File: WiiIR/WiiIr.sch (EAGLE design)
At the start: 18 parts

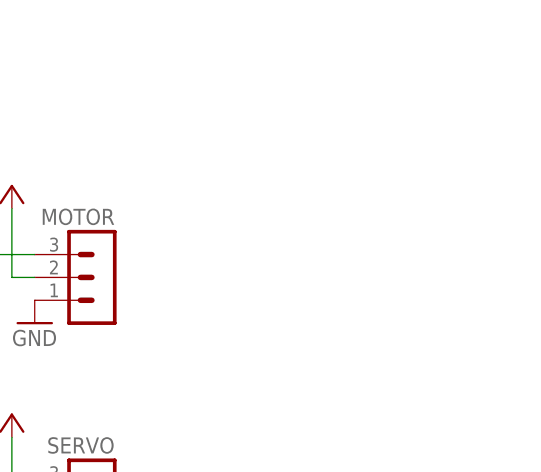
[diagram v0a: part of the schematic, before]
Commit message: XMC Shield servo caps
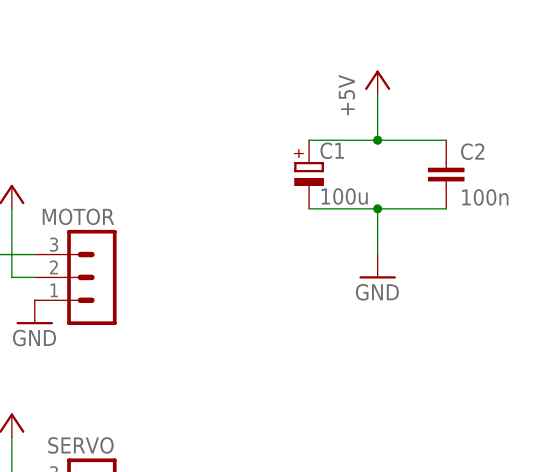
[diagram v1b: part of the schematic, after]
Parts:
- added C1: 100u, resistor:CPOL-EUE2.5-7
- added C2: 100n, resistor:C-EU050-024X044
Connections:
- net +5V: now also C1.+, C2.1
- net GND: now also C1.-, C2.2
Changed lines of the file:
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@@
 <part name="DBG8" library="led" deviceset="LED" device="SQR2X5"/>
 <part name="GND11" library="supply1" deviceset="GND" device=""/>
+<part name="P+5" library="supply1" deviceset="+5V" device=""/>
+<part name="GND6" library="supply1" deviceset="GND" device=""/>
+<part name="C1" library="resistor" deviceset="CPOL-EU" device="E2.5-7" value="100u"/>
+<part name="C2" library="resistor" deviceset="C-EU" device="050-024X044" value="100n"/>
 </parts>
 <sheets>
@@
 <instance part="DBG8" gate="G$1" x="157.48" y="40.64"/>
 <instance part="GND11" gate="1" x="129.54" y="10.16"/>
+<instance part="P+5" gate="1" x="236.22" y="165.1"/>
+<instance part="GND6" gate="1" x="236.22" y="142.24"/>
+<instance part="C1" gate="G$1" x="228.6" y="154.94"/>
+<instance part="C2" gate="G$1" x="243.84" y="154.94"/>
 </instances>
 <busses>
@@
 <wire x1="137.16" y1="149.86" x2="144.78" y2="149.86" width="0.1524" layer="91"/>
 <wire x1="144.78" y1="149.86" x2="144.78" y2="157.48" width="0.1524" layer="91"/>
+</segment>
+<segment>
+<pinref part="C1" gate="G$1" pin="+"/>
+<pinref part="P+5" gate="1" pin="+5V"/>
+<wire x1="228.6" y1="157.48" x2="236.22" y2="157.48" width="0.1524" layer="91"/>
+<wire x1="236.22" y1="157.48" x2="236.22" y2="162.56" width="0.1524" layer="91"/>
+<pinref part="C2" gate="G$1" pin="1"/>
+<wire x1="243.84" y1="157.48" x2="236.22" y2="157.48" width="0.1524" layer="91"/>
+<junction x="236.22" y="157.48"/>
 </segment>
 </net>
@@
 <pinref part="GND11" gate="1" pin="GND"/>
 </segment>
+<segment>
+<pinref part="GND6" gate="1" pin="GND"/>
+<pinref part="C1" gate="G$1" pin="-"/>
+<wire x1="236.22" y1="144.78" x2="236.22" y2="149.86" width="0.1524" layer="91"/>
+<wire x1="236.22" y1="149.86" x2="228.6" y2="149.86" width="0.1524" layer="91"/>
+<pinref part="C2" gate="G$1" pin="2"/>
+<wire x1="243.84" y1="149.86" x2="236.22" y2="149.86" width="0.1524" layer="91"/>
+<junction x="236.22" y="149.86"/>
+</segment>
 </net>

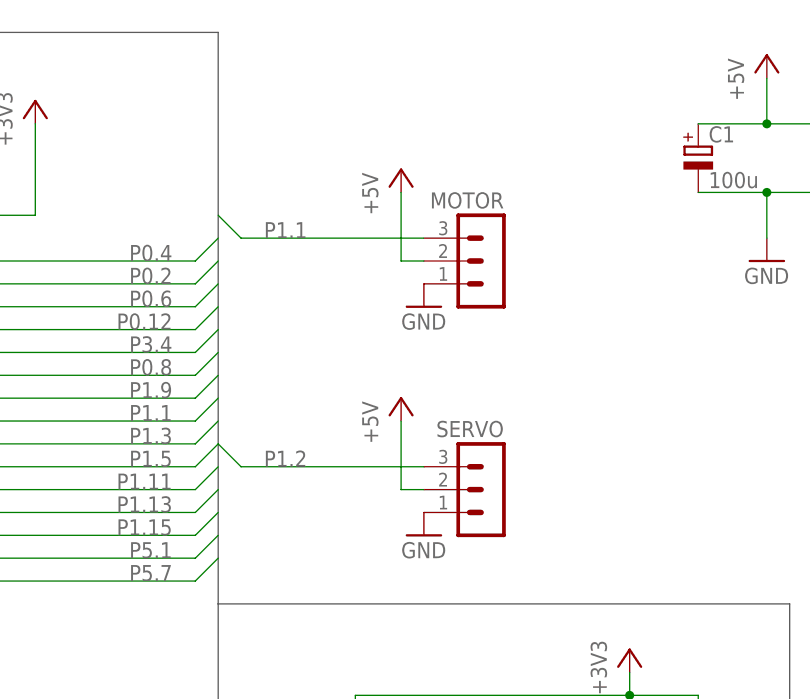
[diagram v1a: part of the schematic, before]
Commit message: Bent pin headers for servo
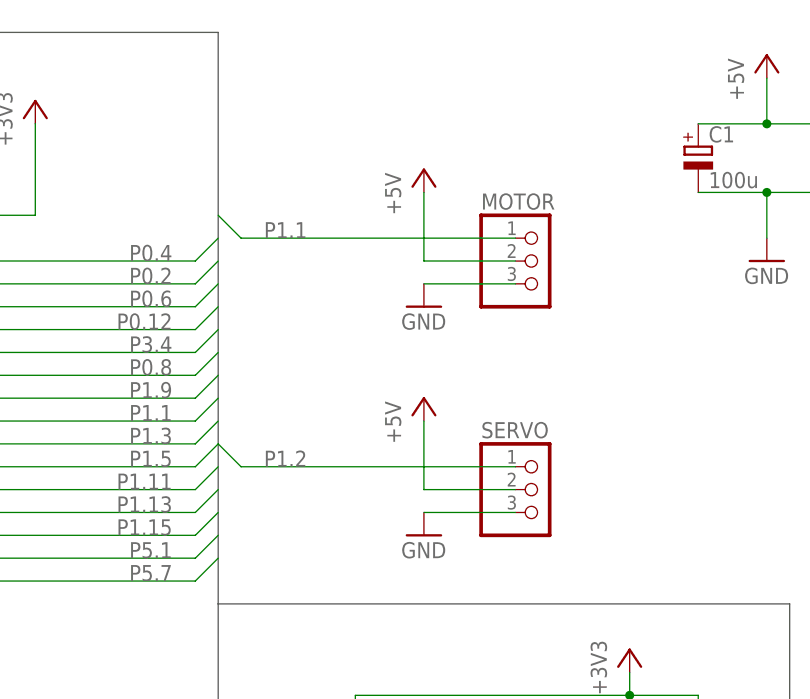
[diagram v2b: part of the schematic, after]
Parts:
- MOTOR, SERVO: device con-lstb:MA03-1 -> pinhead:PINHD-1X3/90
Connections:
- net GND: now also MOTOR.3, SERVO.3; no longer MOTOR.1, SERVO.1
- net P1.1: now also MOTOR.1; no longer MOTOR.3
- net P1.2: now also SERVO.1; no longer SERVO.3
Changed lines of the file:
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@@
 <grid distance="0.1" unitdist="inch" unit="inch" style="lines" multiple="1" display="no" altdistance="0.01" altunitdist="inch" altunit="inch"/>
 <layers>
-<layer number="1" name="Top" color="4" fill="1" visible="no" active="no"/>
-<layer number="16" name="Bottom" color="1" fill="1" visible="no" active="no"/>
-<layer number="17" name="Pads" color="2" fill="1" visible="no" active="no"/>
-<layer number="18" name="Vias" color="2" fill="1" visible="no" active="no"/>
-<layer number="19" name="Unrouted" color="6" fill="1" visible="no" active="no"/>
-<layer number="20" name="Dimension" color="15" fill="1" visible="no" active="no"/>
-<layer number="21" name="tPlace" color="7" fill="1" visible="no" active="no"/>
-<layer number="22" name="bPlace" color="7" fill="1" visible="no" active="no"/>
-<layer number="23" name="tOrigins" color="15" fill="1" visible="no" active="no"/>
-<layer number="24" name="bOrigins" color="15" fill="1" visible="no" active="no"/>
-<layer number="25" name="tNames" color="7" fill="1" visible="no" active="no"/>
-<layer number="26" name="bNames" color="7" fill="1" visible="no" active="no"/>
-<layer number="27" name="tValues" color="7" fill="1" visible="no" active="no"/>
-<layer number="28" name="bValues" color="7" fill="1" visible="no" active="no"/>
+<layer number="1" name="Top" color="4" fill="1" visible="yes" active="no"/>
+<layer number="16" name="Bottom" color="1" fill="1" visible="yes" active="no"/>
+<layer number="17" name="Pads" color="2" fill="1" visible="yes" active="no"/>
+<layer number="18" name="Vias" color="2" fill="1" visible="yes" active="no"/>
+<layer number="19" name="Unrouted" color="6" fill="1" visible="yes" active="no"/>
+<layer number="20" name="Dimension" color="15" fill="1" visible="yes" active="no"/>
+<layer number="21" name="tPlace" color="7" fill="1" visible="yes" active="no"/>
+<layer number="22" name="bPlace" color="7" fill="1" visible="yes" active="no"/>
+<layer number="23" name="tOrigins" color="15" fill="1" visible="yes" active="no"/>
+<layer number="24" name="bOrigins" color="15" fill="1" visible="yes" active="no"/>
+<layer number="25" name="tNames" color="7" fill="1" visible="yes" active="no"/>
+<layer number="26" name="bNames" color="7" fill="1" visible="yes" active="no"/>
+<layer number="27" name="tValues" color="7" fill="1" visible="yes" active="no"/>
+<layer number="28" name="bValues" color="7" fill="1" visible="yes" active="no"/>
 <layer number="29" name="tStop" color="7" fill="3" visible="no" active="no"/>
 <layer number="30" name="bStop" color="7" fill="6" visible="no" active="no"/>
@@
 <layer number="35" name="tGlue" color="7" fill="4" visible="no" active="no"/>
 <layer number="36" name="bGlue" color="7" fill="5" visible="no" active="no"/>
-<layer number="37" name="tTest" color="7" fill="1" visible="no" active="no"/>
-<layer number="38" name="bTest" color="7" fill="1" visible="no" active="no"/>
+<layer number="37" name="tTest" color="7" fill="1" visible="yes" active="no"/>
+<layer number="38" name="bTest" color="7" fill="1" visible="yes" active="no"/>
 <layer number="39" name="tKeepout" color="4" fill="11" visible="no" active="no"/>
 <layer number="40" name="bKeepout" color="1" fill="11" visible="no" active="no"/>
@@
 <layer number="44" name="Drills" color="7" fill="1" visible="no" active="no"/>
 <layer number="45" name="Holes" color="7" fill="1" visible="no" active="no"/>
-<layer number="46" name="Milling" color="3" fill="1" visible="no" active="no"/>
-<layer number="47" name="Measures" color="7" fill="1" visible="no" active="no"/>
-<layer number="48" name="Document" color="7" fill="1" visible="no" active="no"/>
-<layer number="49" name="Reference" color="7" fill="1" visible="no" active="no"/>
-<layer number="51" name="tDocu" color="7" fill="1" visible="no" active="no"/>
-<layer number="52" name="bDocu" color="7" fill="1" visible="no" active="no"/>
+<layer number="46" name="Milling" color="3" fill="1" visible="yes" active="no"/>
+<layer number="47" name="Measures" color="7" fill="1" visible="yes" active="no"/>
+<layer number="48" name="Document" color="7" fill="1" visible="yes" active="no"/>
+<layer number="49" name="Reference" color="7" fill="1" visible="yes" active="no"/>
+<layer number="51" name="tDocu" color="7" fill="1" visible="yes" active="no"/>
+<layer number="52" name="bDocu" color="7" fill="1" visible="yes" active="no"/>
 <layer number="91" name="Nets" color="2" fill="1" visible="yes" active="yes"/>
 <layer number="92" name="Busses" color="1" fill="1" visible="yes" active="yes"/>
@@
 <part name="P+4" library="supply1" deviceset="+5V" device=""/>
 <part name="IR_CAM" library="con-harting-ml" deviceset="ML10" device=""/>
-<part name="MOTOR" library="con-lstb" deviceset="MA03-1" device=""/>
 <part name="FRAME1" library="frames" deviceset="A4L-LOC" device=""/>
 <part name="GND7" library="supply1" deviceset="GND" device=""/>
 <part name="P+9" library="supply1" deviceset="+5V" device=""/>
-<part name="SERVO" library="con-lstb" deviceset="MA03-1" device=""/>
 <part name="GND10" library="supply1" deviceset="GND" device=""/>
 <part name="P+11" library="supply1" deviceset="+5V" device=""/>
@@
 <part name="C1" library="resistor" deviceset="CPOL-EU" device="E2.5-7" value="100u"/>
 <part name="C2" library="resistor" deviceset="C-EU" device="050-024X044" value="100n"/>
+<part name="MOTOR" library="pinhead" deviceset="PINHD-1X3" device="/90"/>
+<part name="SERVO" library="pinhead" deviceset="PINHD-1X3" device="/90"/>
 </parts>
 <sheets>
@@
 <instance part="P+4" gate="1" x="144.78" y="160.02"/>
 <instance part="IR_CAM" gate="G$1" x="205.74" y="78.74"/>
-<instance part="MOTOR" gate="G$1" x="205.74" y="142.24" rot="MR0"/>
 <instance part="FRAME1" gate="G$1" x="0" y="0"/>
 <instance part="GND7" gate="1" x="198.12" y="137.16"/>
-<instance part="P+9" gate="1" x="195.58" y="152.4"/>
-<instance part="SERVO" gate="G$1" x="205.74" y="116.84" rot="MR0"/>
+<instance part="P+9" gate="1" x="198.12" y="152.4"/>
 <instance part="GND10" gate="1" x="198.12" y="111.76"/>
-<instance part="P+11" gate="1" x="195.58" y="127"/>
+<instance part="P+11" gate="1" x="198.12" y="127"/>
 <instance part="BLUETOOTH" gate="G$1" x="38.1" y="71.12" smashed="yes">
 <attribute name="VALUE" x="36.83" y="58.42" size="1.778" layer="96"/>
@@
 <instance part="C1" gate="G$1" x="228.6" y="154.94"/>
 <instance part="C2" gate="G$1" x="243.84" y="154.94"/>
+<instance part="MOTOR" gate="A" x="210.82" y="142.24"/>
+<instance part="SERVO" gate="A" x="210.82" y="116.84"/>
 </instances>
 <busses>
@@
 <net name="+5V" class="0">
 <segment>
-<pinref part="MOTOR" gate="G$1" pin="2"/>
 <pinref part="P+9" gate="1" pin="+5V"/>
-<wire x1="198.12" y1="142.24" x2="195.58" y2="142.24" width="0.1524" layer="91"/>
-<wire x1="195.58" y1="142.24" x2="195.58" y2="149.86" width="0.1524" layer="91"/>
-</segment>
-<segment>
-<pinref part="SERVO" gate="G$1" pin="2"/>
+<wire x1="198.12" y1="142.24" x2="198.12" y2="149.86" width="0.1524" layer="91"/>
+<pinref part="MOTOR" gate="A" pin="2"/>
+<wire x1="198.12" y1="142.24" x2="208.28" y2="142.24" width="0.1524" layer="91"/>
+</segment>
+<segment>
 <pinref part="P+11" gate="1" pin="+5V"/>
-<wire x1="198.12" y1="116.84" x2="195.58" y2="116.84" width="0.1524" layer="91"/>
-<wire x1="195.58" y1="116.84" x2="195.58" y2="124.46" width="0.1524" layer="91"/>
+<wire x1="198.12" y1="116.84" x2="198.12" y2="124.46" width="0.1524" layer="91"/>
+<pinref part="SERVO" gate="A" pin="2"/>
+<wire x1="208.28" y1="116.84" x2="198.12" y2="116.84" width="0.1524" layer="91"/>
 </segment>
 <segment>
@@
 <junction x="142.24" y="104.14"/>
 <junction x="142.24" y="101.6"/>
-</segment>
-<segment>
-<pinref part="MOTOR" gate="G$1" pin="1"/>
-<pinref part="GND7" gate="1" pin="GND"/>
-</segment>
-<segment>
-<pinref part="SERVO" gate="G$1" pin="1"/>
-<pinref part="GND10" gate="1" pin="GND"/>
 </segment>
 <segment>
@@
 <junction x="236.22" y="149.86"/>
 </segment>
+<segment>
+<pinref part="MOTOR" gate="A" pin="3"/>
+<pinref part="GND7" gate="1" pin="GND"/>
+<wire x1="208.28" y1="139.7" x2="198.12" y2="139.7" width="0.1524" layer="91"/>
+</segment>
+<segment>
+<pinref part="SERVO" gate="A" pin="3"/>
+<pinref part="GND10" gate="1" pin="GND"/>
+<wire x1="208.28" y1="114.3" x2="198.12" y2="114.3" width="0.1524" layer="91"/>
+</segment>
 </net>
 <net name="P2.1" class="0">
@@
 </segment>
 <segment>
-<pinref part="SERVO" gate="G$1" pin="3"/>
 <wire x1="175.26" y1="121.92" x2="177.8" y2="119.38" width="0.1524" layer="91"/>
-<wire x1="177.8" y1="119.38" x2="198.12" y2="119.38" width="0.1524" layer="91"/>
 <label x="180.34" y="119.38" size="1.778" layer="95"/>
+<pinref part="SERVO" gate="A" pin="1"/>
+<wire x1="177.8" y1="119.38" x2="208.28" y2="119.38" width="0.1524" layer="91"/>
 </segment>
 </net>
@@
 </segment>
 <segment>
-<pinref part="MOTOR" gate="G$1" pin="3"/>
 <wire x1="175.26" y1="147.32" x2="177.8" y2="144.78" width="0.1524" layer="91"/>
-<wire x1="177.8" y1="144.78" x2="198.12" y2="144.78" width="0.1524" layer="91"/>
 <label x="180.34" y="144.78" size="1.778" layer="95"/>
-</segment>
-</net>
+<pinref part="MOTOR" gate="A" pin="1"/>
+<wire x1="177.8" y1="144.78" x2="208.28" y2="144.78" width="0.1524" layer="91"/>
+</segment>
+</net>
